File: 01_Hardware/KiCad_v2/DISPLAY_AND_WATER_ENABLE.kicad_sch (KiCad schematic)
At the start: 30 parts, among them J700 JST_B4B, J701 JST_B4B, Q700 BSS314PE, Q701 BSS314PE, Q702 NVTA7002NT1G, Q703 NVTA7002NT1G

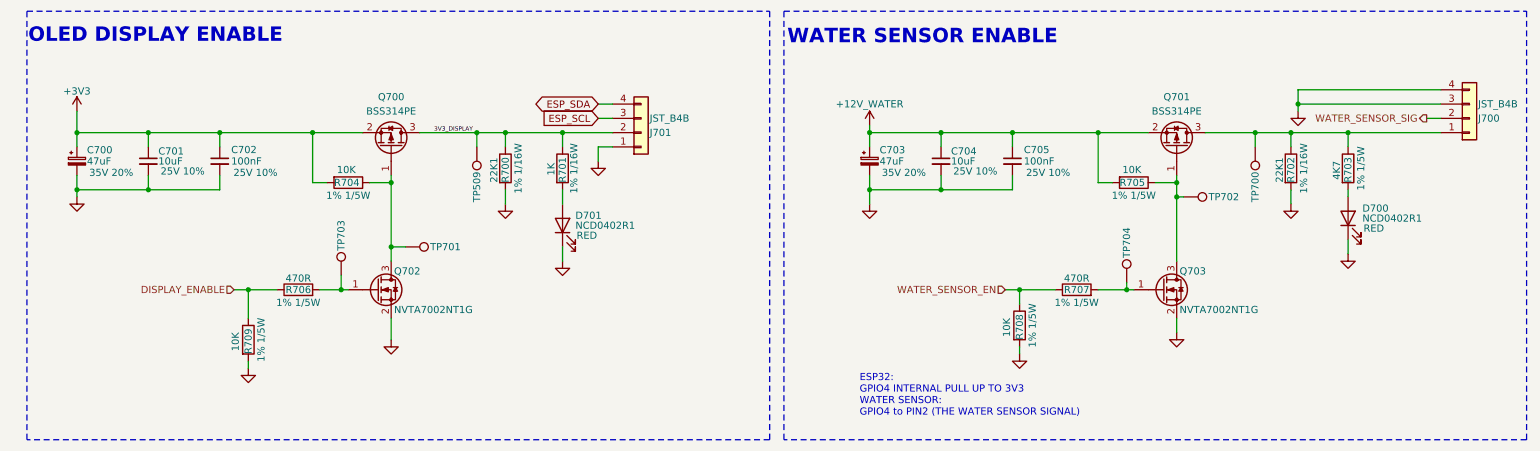
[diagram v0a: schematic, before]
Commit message: BOM done, except connectors/thermistor/button -> Will re-check BOM before sending to manufacturing
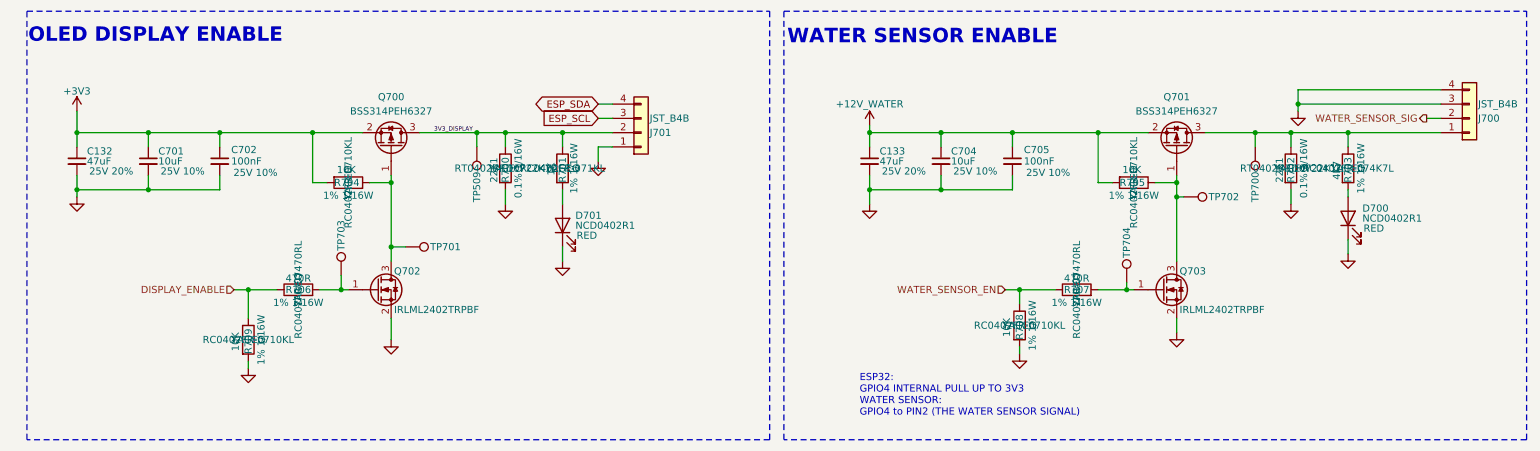
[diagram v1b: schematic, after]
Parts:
- removed C700, C703: 47uF, Capacitor_SMD:CP_Elec_6.3x5.8, symbol Device:C_Polarized_Small
- added C132, C133: 47uF, Capacitor_SMD:C_1206_3216Metric, symbol Device:C_Small
- C701, C704: Manufacturer Murata Electronics -> Murata Electronics
- C702, C705: Manufacturer Samsung Electro-Mechanics -> Samsung Electro-Mechanics
- D700, D701: footprint Custom_Global_Footprints:SML-P13PTT_LED_0402_1005Metric -> LED_SMD:LED_0402_1005Metric
- Q700, Q701: value BSS314PE -> BSS314PEH6327; Link (none) -> https://jlcpcb.com/partdetail/InfineonTechnologies-BSS314PE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; Manufacturer (none) -> Infineon Technologies; Manufacturer Part Number (none) -> BSS314PEH6327
- Q702, Q703: value NVTA7002NT1G -> IRLML2402TRPBF; footprint Custom_Global_Footprints:NVTA7002N -> Package_TO_SOT_SMD:SOT-23; Link (none) -> https://jlcpcb.com/partdetail/InfineonTechnologies-IRLML240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; Manufacturer (none) -> Infineon Technologies; Manufacturer Part Number (none) -> IRLML2402TRPBF
- R700, R702: Manufacturer (none) -> YAGEO; Manufacturer Part Number (none) -> RT0402BRD0722K1L
- R701: Manufacturer (none) -> YAGEO; Manufacturer Part Number (none) -> RC0402FR-071KL
- R703: Manufacturer (none) -> YAGEO; Manufacturer Part Number (none) -> RC0402FR-074K7L
- R704, R705, R708, R709: Manufacturer (none) -> YAGEO; Manufacturer Part Number (none) -> RC0402FR-0710KL
- R706, R707: Manufacturer (none) -> YAGEO; Manufacturer Part Number (none) -> RC0402FR-07470RL
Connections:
- net +12V_WATER: now also C133.1
- net +3V3: now also C132.1
- net GND: now also C132.2, C133.2

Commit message: USB-C and Serial PCB routing done
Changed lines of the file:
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@@
 					(size 1.27 1.27)
 				)
+				(hide yes)
 			)
 		)
@@
 					(size 1.27 1.27)
 				)
+				(hide yes)
 			)
 		)
@@
 					(size 1.27 1.27)
 				)
+				(hide yes)
 			)
 		)
@@
 					(size 1.27 1.27)
 				)
+				(hide yes)
 			)
 		)
@@
 					(size 1.27 1.27)
 				)
+				(hide yes)
 			)
 		)
@@
 					(size 1.27 1.27)
 				)
+				(hide yes)
 			)
 		)
@@
 					(size 1.27 1.27)
 				)
+				(hide yes)
 			)
 		)
@@
 					(size 1.27 1.27)
 				)
+				(hide yes)
 			)
 		)
@@
 					(size 1.27 1.27)
 				)
+				(hide yes)
 			)
 		)
@@
 					(size 1.27 1.27)
 				)
+				(hide yes)
 			)
 		)
@@
 					(size 1.27 1.27)
 				)
+				(hide yes)
 			)
 		)
@@
 					(size 1.27 1.27)
 				)
+				(hide yes)
 			)
 		)
@@
 					(size 1.27 1.27)
 				)
+				(hide yes)
 			)
 		)
@@
 					(size 1.27 1.27)
 				)
+				(hide yes)
 			)
 		)
@@
 					(size 1.27 1.27)
 				)
+				(hide yes)
 			)
 		)
@@
 					(size 1.27 1.27)
 				)
+				(hide yes)
 			)
 		)
@@
 					(size 1.27 1.27)
 				)
+				(hide yes)
 			)
 		)
@@
 					(size 1.27 1.27)
 				)
+				(hide yes)
 			)
 		)
@@
 					(size 1.27 1.27)
 				)
+				(hide yes)
 			)
 		)
@@
 					(size 1.27 1.27)
 				)
+				(hide yes)
 			)
 		)
@@
 					(size 1.27 1.27)
 				)
+				(hide yes)
 			)
 		)
@@
 					(size 1.27 1.27)
 				)
+				(hide yes)
 			)
 		)
@@
 					(size 1.27 1.27)
 				)
+				(hide yes)
 			)
 		)
@@
 					(size 1.27 1.27)
 				)
+				(hide yes)
 			)
 		)
@@
 					(size 1.27 1.27)
 				)
+				(hide yes)
 			)
 		)
@@
 					(size 1.27 1.27)
 				)
+				(hide yes)
 			)
 		)
@@
 					(size 1.27 1.27)
 				)
+				(hide yes)
 			)
 		)
@@
 					(size 1.27 1.27)
 				)
+				(hide yes)
 			)
 		)
@@
 					(size 1.27 1.27)
 				)
+				(hide yes)
 			)
 		)
@@
 					(size 1.27 1.27)
 				)
+				(hide yes)
 			)
 		)
@@
 					(size 1.27 1.27)
 				)
+				(hide yes)
 			)
 		)
@@
 					(size 1.27 1.27)
 				)
+				(hide yes)
 			)
 		)
@@
 					(size 1.27 1.27)
 				)
+				(hide yes)
 			)
 		)
@@
 					(size 1.27 1.27)
 				)
+				(hide yes)
 			)
 		)
@@
 					(size 1.27 1.27)
 				)
+				(hide yes)
 			)
 		)
@@
 					(size 1.27 1.27)
 				)
+				(hide yes)
 			)
 		)
@@
 					(size 1.27 1.27)
 				)
+				(hide yes)
 			)
 		)
@@
 					(size 1.27 1.27)
 				)
+				(hide yes)
 			)
 		)
@@
 					(size 1.27 1.27)
 				)
+				(hide yes)
 			)
 		)
@@
 					(size 1.27 1.27)
 				)
-			)
-		)
+				(hide yes)
+			)
+		)
